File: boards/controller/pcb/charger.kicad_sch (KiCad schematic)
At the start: 33 parts, among them J4001 Battery, U4001 BQ25792RQMR

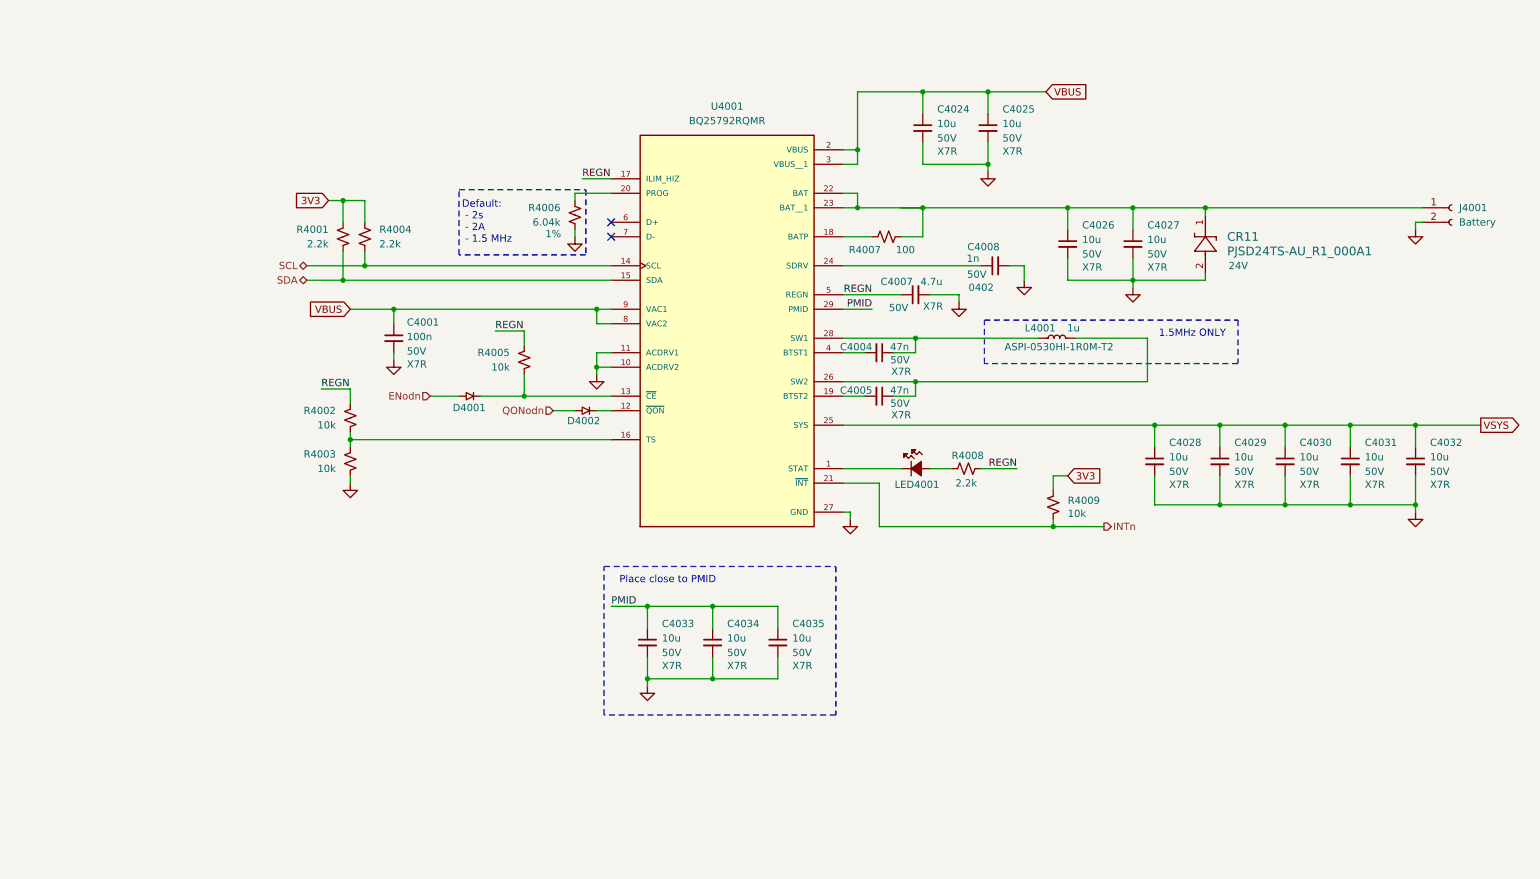
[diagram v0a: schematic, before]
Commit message: controller: pcb: Update schematic
Signed-off-by: Nicholas Loehrke <nicholasnloehrke@gmail.com>
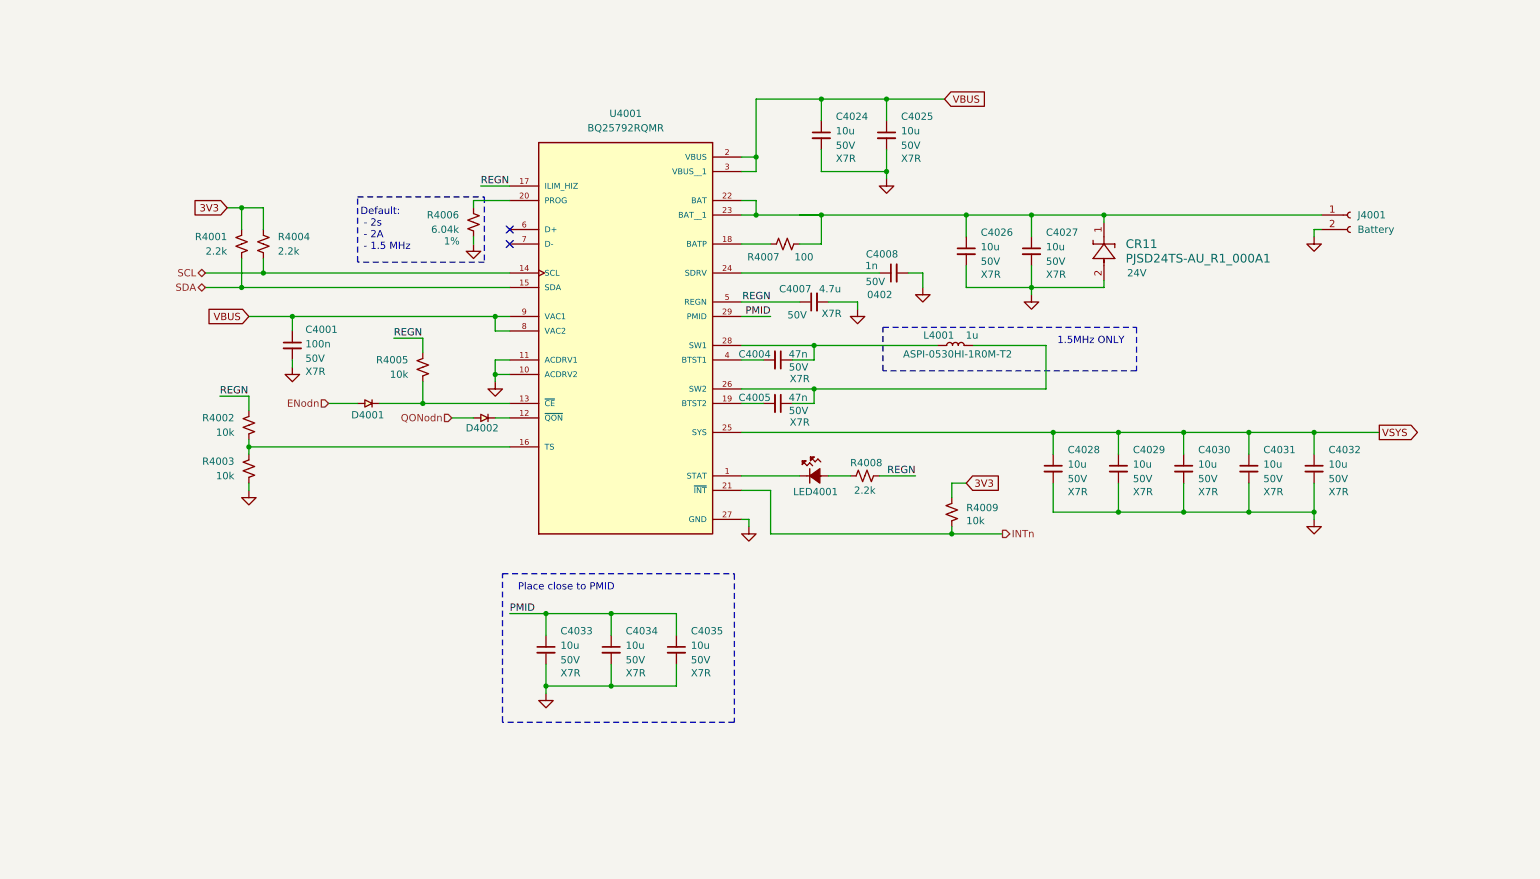
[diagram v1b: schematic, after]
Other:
- moved on the sheet: C4001, C4004, C4005, C4007, C4008, C4024, C4025, C4026, C4027, C4028, C4029, C4030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

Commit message: controller: pcb: Update schematic
- add VBAT sense circuit
- add BLS power pmos
- assign BLS GPIO

Signed-off-by: Nicholas Loehrke <nicholasnloehrke@gmail.com>
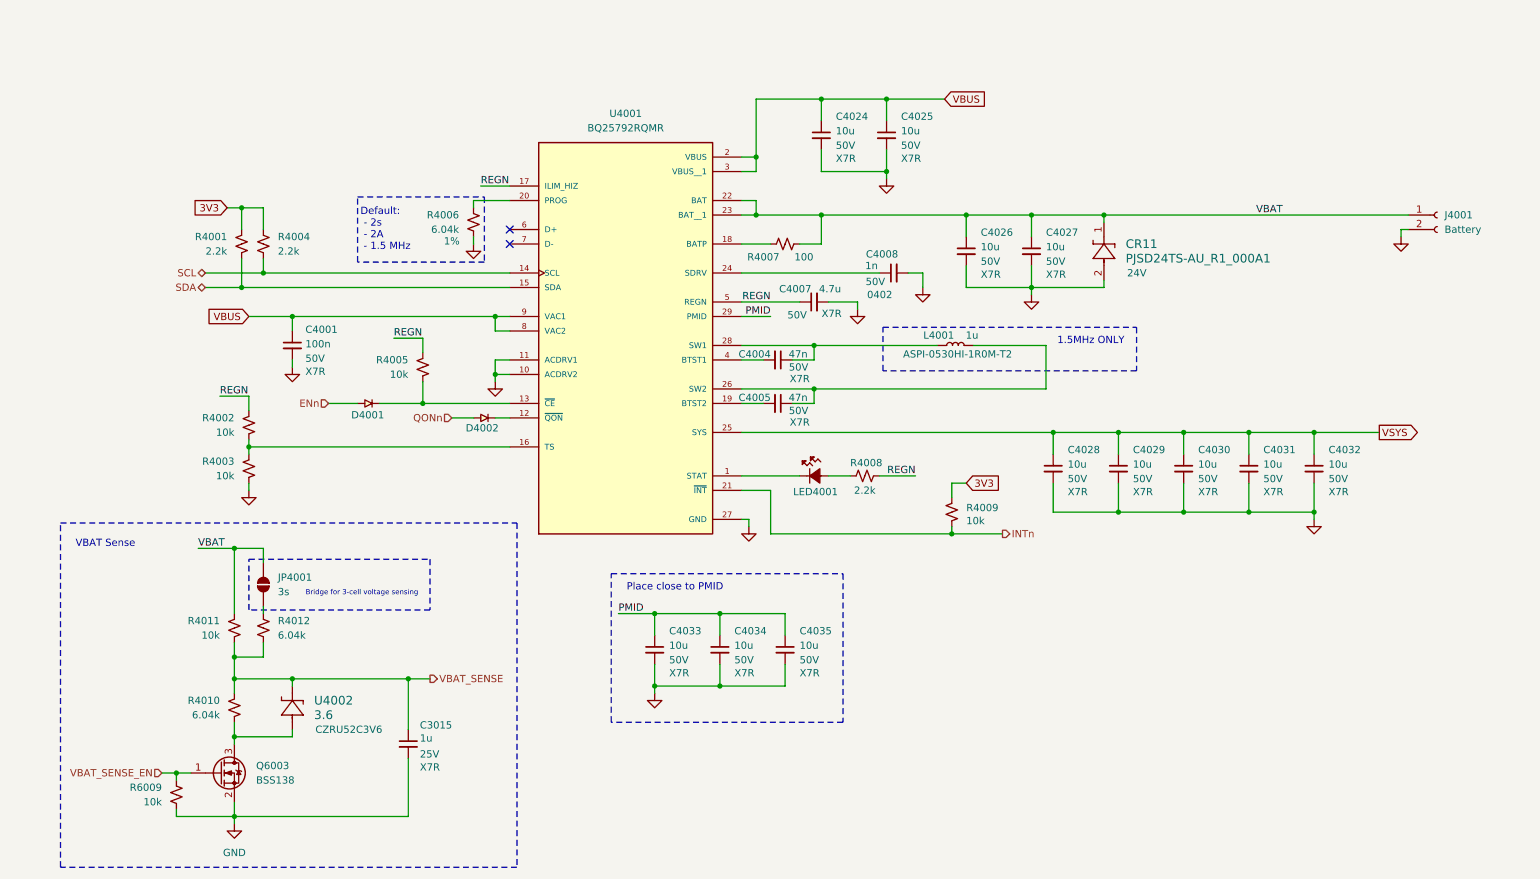
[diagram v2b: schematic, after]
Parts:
- added C3015: 1u, symbol Device:C_Small
- added JP4001: 3s, symbol Jumper:SolderJumper_2_Open
- added Q6003: BSS138, Package_TO_SOT_SMD:SOT-23, symbol Transistor_FET:BSS138
- added R4010, R4012: 6.04k, symbol Device:R_Small_US
- added R4011, R6009: 10k, symbol Device:R_Small_US
- added U4002: 3.6, CZRU, symbol CZRU52C3V6:CZRU52C3V6
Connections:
- net GND: now also C3015.2, Q6003.2 (S), R6009.2
- net VBAT: now reaches C4026.1, C4027.1, CR11.1, J4001.1 (Pin_1), R4007.2, U4001.22 (BAT), U4001.23 (BAT__1)
- net VBAT: now also JP4001.2 (B), R4011.1
- net ENodn renamed ENn
- net QONodn renamed QONn
- new net: Q6003.3 (D), R4010.2, U4002.2
- new net: JP4001.1 (A), R4012.1
- new net VBAT_SENSE: C3015.1, R4010.1, R4011.2, R4012.2, U4002.1
- new net VBAT_SENSE_EN: Q6003.1 (G), R6009.1
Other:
- note added: "Bridge for 3-cell voltage sensing"
- note added: "VBAT Sense"
- moved on the sheet: C4033, C4034, C4035, J4001

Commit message: controller: pcb: Update schematic
Signed-off-by: Nicholas Loehrke <nicholasnloehrke@gmail.com>
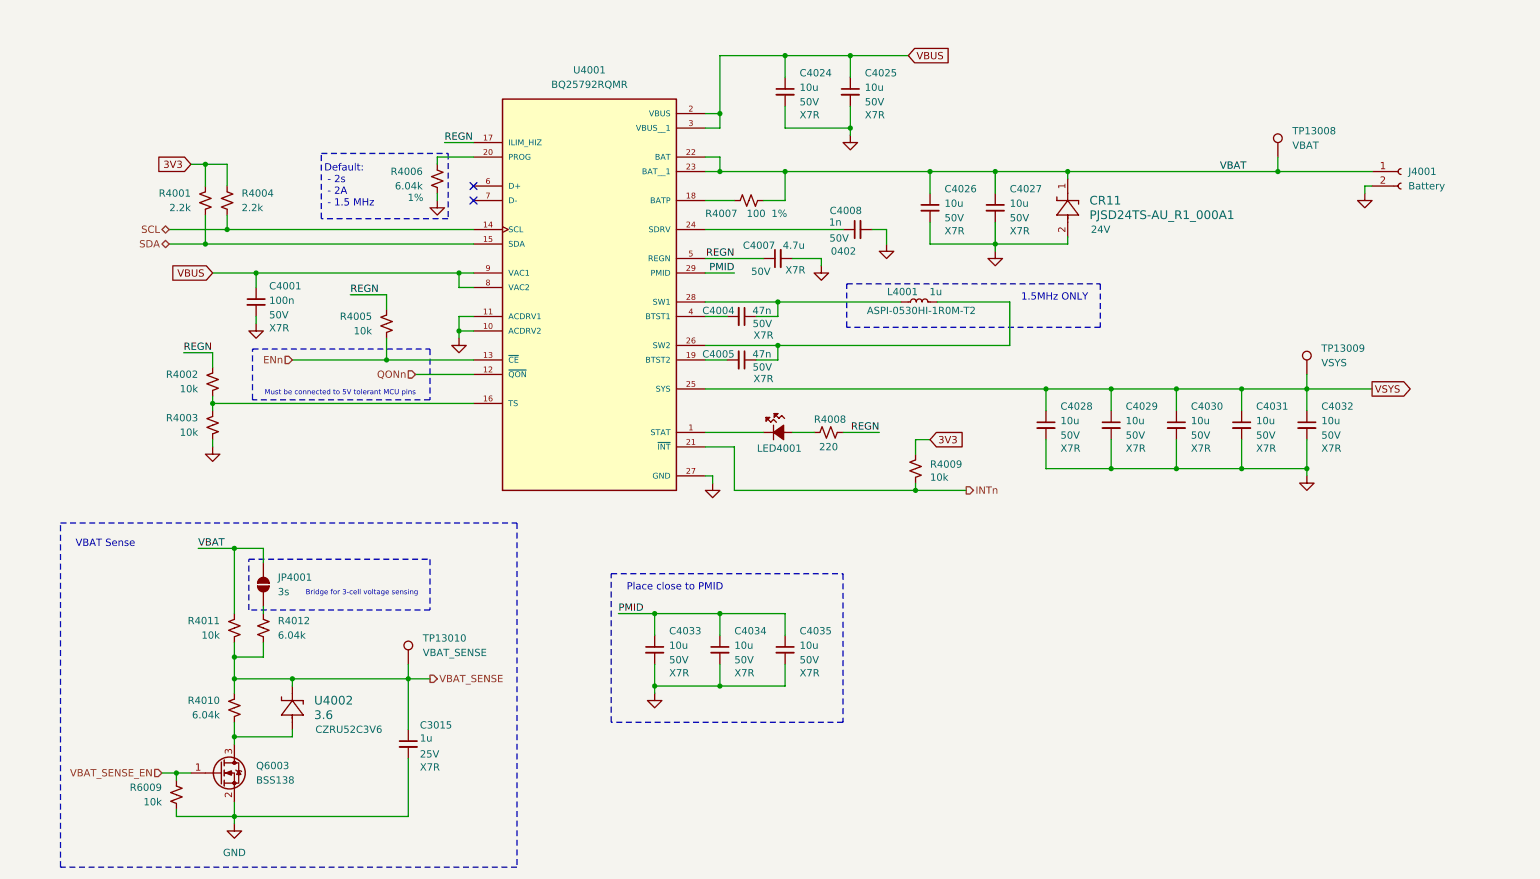
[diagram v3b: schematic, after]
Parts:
- removed D4001, D4002: CUS10S30_H3F, USC_TOS, symbol CUS10S30_H3F:CUS10S30_H3F
- added TP13008: VBAT, symbol Connector:TestPoint
- added TP13009: VSYS, symbol Connector:TestPoint
- added TP13010: VBAT_SENSE, symbol Connector:TestPoint
- R4007: Tolerance (none) -> 1%
- R4008: value 2.2k -> 220
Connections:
- net ENn: now also R4005.2, U4001.13 (~{CE})
- net QONn: now also U4001.12 (~{QON})
- net VBAT: now also TP13008.1
- net VBAT_SENSE: now also TP13010.1
- net VSYS: now also TP13009.1
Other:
- note added: "Must be connected to 5V tolerant MCU pins"
- moved on the sheet: C4001, C4004, C4005, C4007, C4008, C4024, C4025, C4026, C4027, C4028, C4029, C4030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

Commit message: controller: pcb: Update schematic + layout
Signed-off-by: Nicholas Loehrke <nicholasnloehrke@gmail.com>
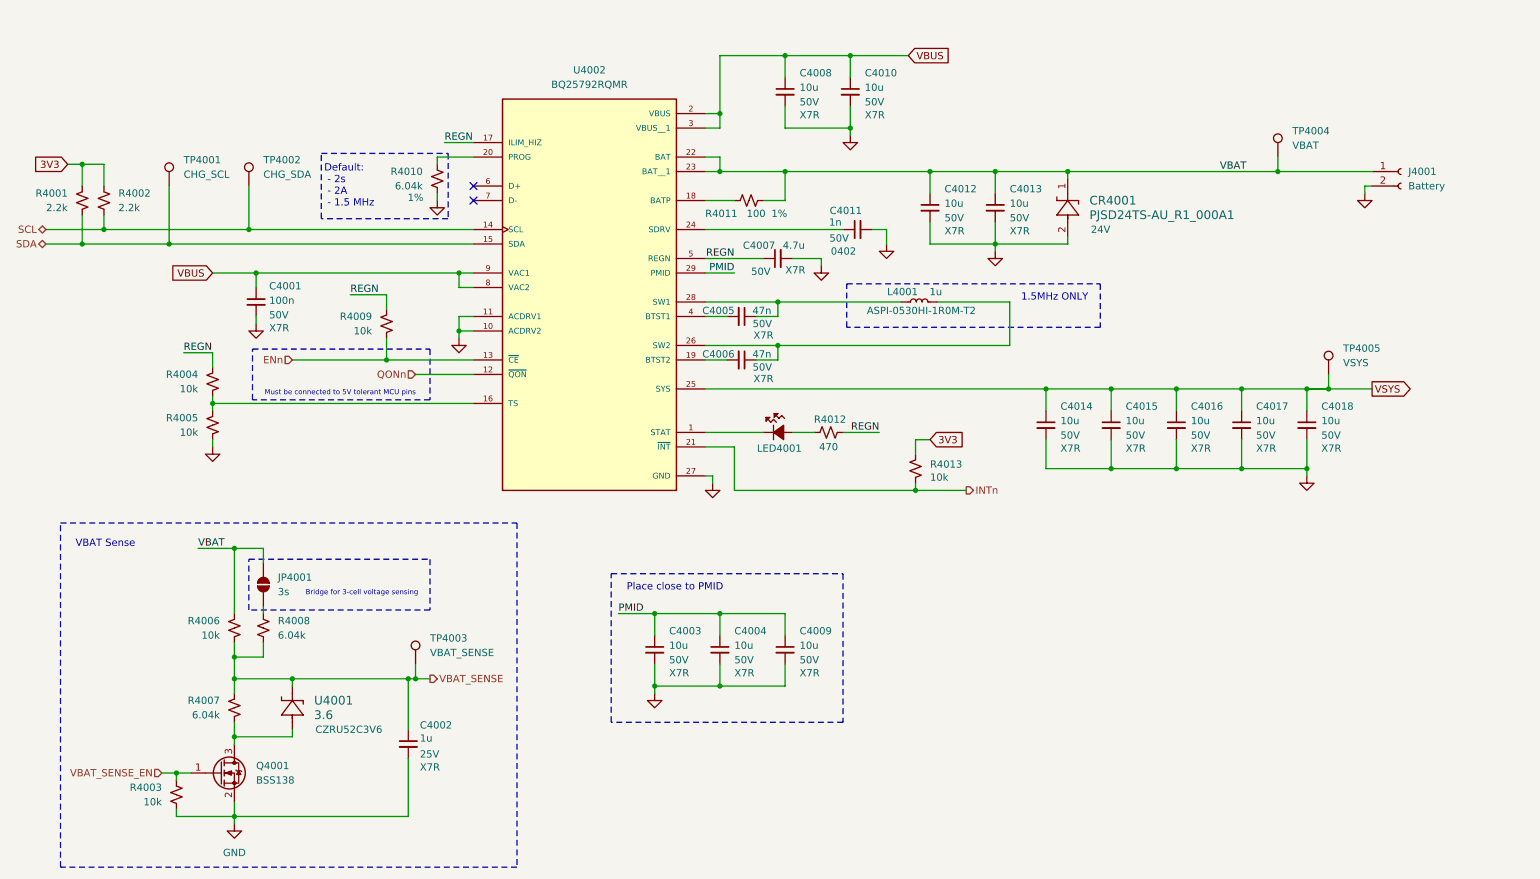
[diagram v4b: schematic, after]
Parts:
- added TP4001: CHG_SCL, TestPoint:TestPoint_Pad_D1.0mm, symbol Connector:TestPoint
- added TP4002: CHG_SDA, TestPoint:TestPoint_Pad_D1.0mm, symbol Connector:TestPoint
- C4001: footprint (none) -> Capacitor_SMD:C_0402_1005Metric
- C4002: renamed from C3015; footprint (none) -> Capacitor_SMD:C_0603_1608Metric
- C4003: renamed from C4033; footprint (none) -> Capacitor_SMD:C_1210_3225Metric
- C4004: renamed from C4034; footprint (none) -> Capacitor_SMD:C_1210_3225Metric
- C4005: renamed from C4004; footprint (none) -> Capacitor_SMD:C_0402_1005Metric
- C4006: renamed from C4005; footprint (none) -> Capacitor_SMD:C_0402_1005Metric
- C4007: footprint (none) -> Capacitor_SMD:C_0805_2012Metric
- C4008: renamed from C4024; footprint (none) -> Capacitor_SMD:C_1210_3225Metric
- C4009: renamed from C4035; footprint (none) -> Capacitor_SMD:C_1210_3225Metric
- C4010: renamed from C4025; footprint (none) -> Capacitor_SMD:C_1210_3225Metric
- C4011: renamed from C4008; footprint (none) -> Capacitor_SMD:C_0402_1005Metric
- C4012: renamed from C4026; footprint (none) -> Capacitor_SMD:C_1210_3225Metric
- C4013: renamed from C4027; footprint (none) -> Capacitor_SMD:C_1210_3225Metric
- C4014: renamed from C4028; footprint (none) -> Capacitor_SMD:C_1210_3225Metric
- C4015: renamed from C4029; footprint (none) -> Capacitor_SMD:C_1210_3225Metric
- C4016: renamed from C4030; footprint (none) -> Capacitor_SMD:C_1210_3225Metric
- C4017: renamed from C4031; footprint (none) -> Capacitor_SMD:C_1210_3225Metric
- C4018: renamed from C4032; footprint (none) -> Capacitor_SMD:C_1210_3225Metric
- CR4001: renamed from CR11; footprint CR_SOD-523_PNJ -> PJSD24TS-AU_R1_000A1:PJSD24TS-AU_R1_000A1
- J4001: footprint (none) -> XT30:AMASS_XT30U-F_1x02_P5.0mm_Vertical
- JP4001: footprint (none) -> Jumper:SolderJumper-2_P1.3mm_Open_RoundedPad1.0x1.5mm
- L4001: footprint ASPI-0530HI-1R0M-T2:IND_ASPI-0530HI-1R0M-T2 -> ASPI-0530HI-1R0M-T2:ASPI-0530HI-1R0M-T2
- LED4001: footprint LED_B1911PG--20D000514U1930_HVK -> B1911PG--20D000514U1930:B1911PG--20D000514U1930
- R4001: footprint (none) -> Resistor_SMD:R_0603_1608Metric
- R4002: renamed from R4004; footprint (none) -> Resistor_SMD:R_0603_1608Metric
- R4003: renamed from R6009; footprint (none) -> Resistor_SMD:R_0402_1005Metric
- R4004: renamed from R4002; footprint (none) -> Resistor_SMD:R_0402_1005Metric
- R4005: renamed from R4003; footprint (none) -> Resistor_SMD:R_0402_1005Metric
- R4006: renamed from R4011; footprint (none) -> Resistor_SMD:R_0402_1005Metric
- R4007: renamed from R4010; footprint (none) -> Resistor_SMD:R_0402_1005Metric
- R4008: renamed from R4012; footprint (none) -> Resistor_SMD:R_0402_1005Metric
- R4009: renamed from R4005; footprint (none) -> Resistor_SMD:R_0402_1005Metric
- R4010: renamed from R4006; footprint (none) -> Resistor_SMD:R_0402_1005Metric
- R4011: renamed from R4007; footprint (none) -> Resistor_SMD:R_0402_1005Metric
- R4012: renamed from R4008; value 220 -> 470; footprint (none) -> Resistor_SMD:R_0603_1608Metric
- R4013: renamed from R4009; footprint (none) -> Resistor_SMD:R_0402_1005Metric
- TP4003: renamed from TP13010; footprint (none) -> TestPoint:TestPoint_Pad_D1.0mm
- TP4004: renamed from TP13008; footprint (none) -> TestPoint:TestPoint_Pad_D1.0mm
- TP4005: renamed from TP13009; footprint (none) -> TestPoint:TestPoint_Pad_D1.0mm
- U4001: renamed from U4002; footprint CZRU -> CZRU52C3V6:CZRU52C3V6
- U4002: renamed from U4001; footprint BQ25792RQMR:QFN40P400X400X100-29N -> BQ25792RQMR:BQ25792RQMR
- renumbered Q6003 to Q4001
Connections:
- net SCL: now also TP4002.1
- net SDA: now also TP4001.1
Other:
- moved on the sheet: R4001, R4002, TP4003, TP4005
